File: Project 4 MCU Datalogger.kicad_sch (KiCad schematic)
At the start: 0 parts

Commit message: Setup of EESCHEMA
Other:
- title: (none) -> ${project_name}
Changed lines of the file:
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@@
 	(generator_version "9.0")
 	(paper "A4")
+	(title_block
+		(title "${project_name}")
+		(date "2026-06-19")
+	)
 	(sheet_instances
 		(path "/"

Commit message: Finished placiong symbols
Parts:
- added BT1: Battery, symbol Device:Battery
- added C1, C2, C3, C4: C, symbol Device:C
- added C5: C_Polarized, symbol Device:C_Polarized
- added D1, D2: LED, symbol Device:LED
- added H1, H2, H3, H4: MountingHole, symbol Mechanical:MountingHole
- added R1, R2, R3, R4, R5, R6, R7: R, symbol Device:R
- added U1, U2: 24LC1025, symbol Memory_EEPROM:24LC1025
- added U3: ATMEGA328PB-AUR, 32A_MCH, symbol 2026-06-19_09-47-19:ATMEGA328PB-AUR
- added U4: ds1337s+, 21-0041B_8_MXM, symbol 2026-06-19_09-48-52:ds1337s+
- added Y1, Y2: Crystal, symbol Device:Crystal

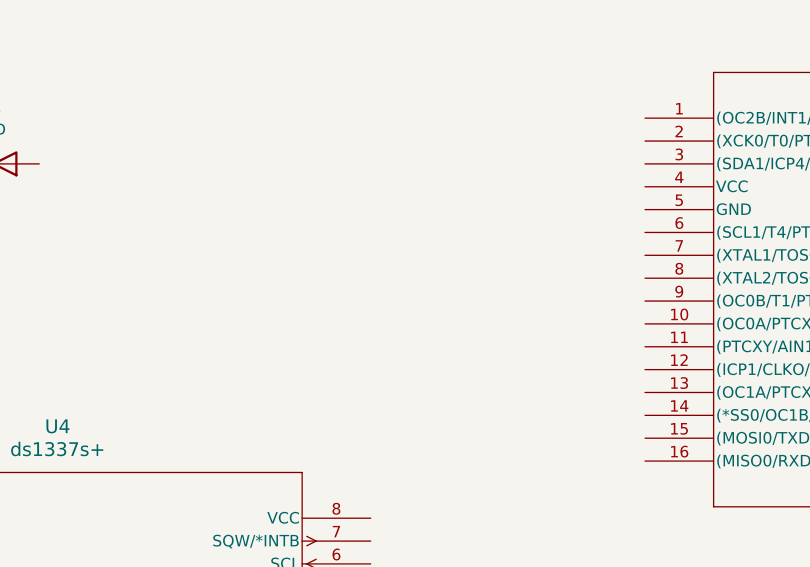
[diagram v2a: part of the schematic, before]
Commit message: Adding second sheet in EESCHEMA
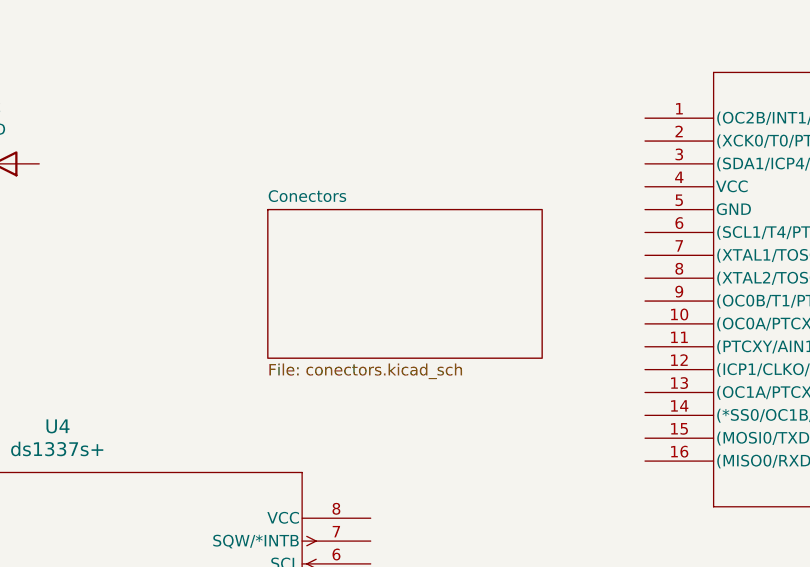
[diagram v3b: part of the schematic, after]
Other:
- added sheet Conectors (conectors.kicad_sch)
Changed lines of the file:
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@@
+		)
+	)
+	(sheet
+		(at 107.95 127)
+		(size 30.48 16.51)
+		(exclude_from_sim no)
+		(in_bom yes)
+		(on_board yes)
+		(dnp no)
+		(fields_autoplaced yes)
+		(stroke
+			(width 0.1524)
+			(type solid)
+		)
+		(fill
+			(color 0 0 0 0.0000)
+		)
+		(property "Sheetname" "Conectors"
+			(at 107.95 126.2884 0)
+			(effects
+				(font
+					(size 1.27 1.27)
+				)
+				(justify left bottom)
+			)
+		)
+		(property "Sheetfile" "conectors.kicad_sch"
+			(at 107.95 144.0946 0)
+			(effects
+				(font
+					(size 1.27 1.27)
+				)
+				(justify left top)
+			)
+		)
+		(instances
+			(project "Project 4 MCU Datalogger"
+				(path "/7724fa4a-e87e-4e24-9bef-a23a7b16e103"
+					(page "2")
+				)
+			)
 		)
 	)
